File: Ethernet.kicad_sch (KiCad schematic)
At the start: 47 parts, among them J2 RJ45_Hanrun_HR911105A_Horizon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, U2 DP83848C, U3 AMS1117-3.3, Y2 WTL7K85438FO

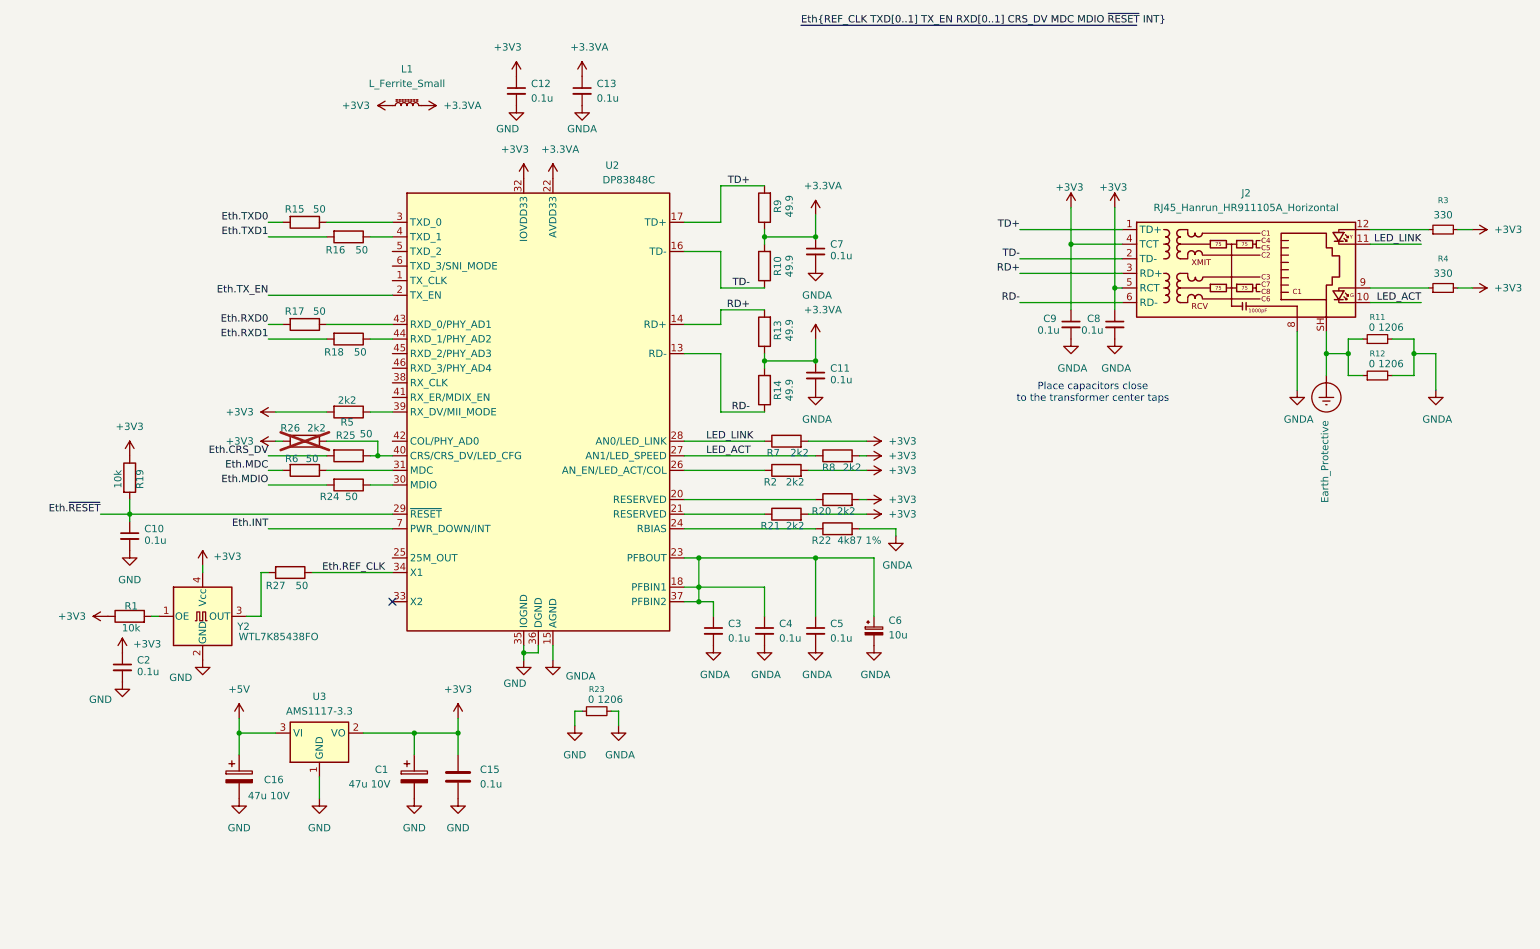
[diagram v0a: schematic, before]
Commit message: Ethernet W55000 controller added
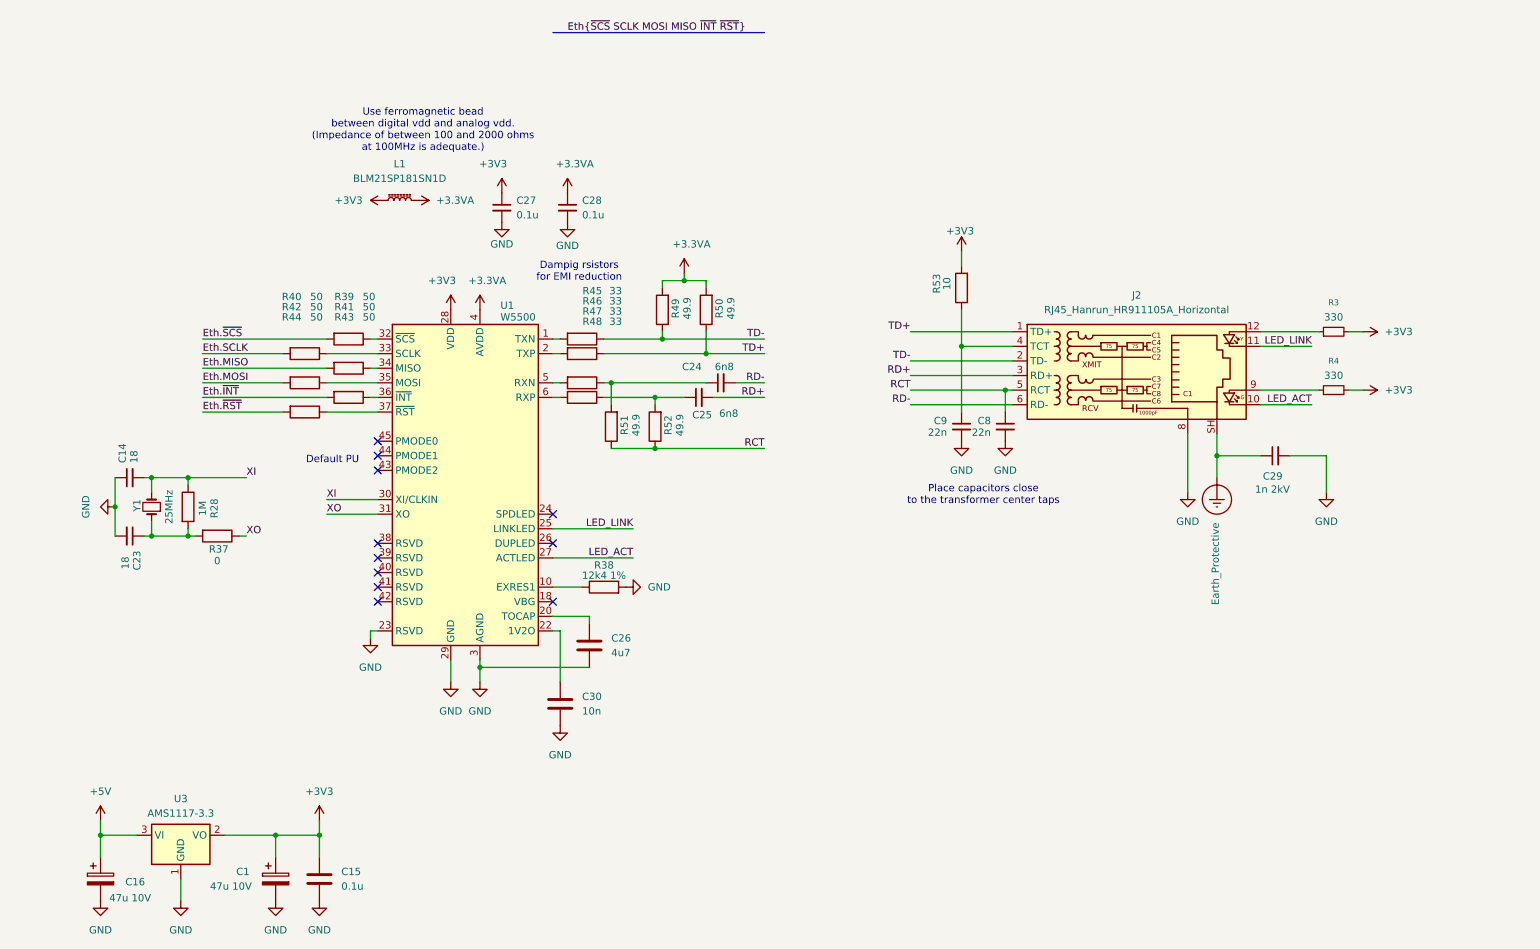
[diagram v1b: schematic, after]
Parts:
- removed C10, C11, C12, C13, C2, C3, C4, C5, C7: 0.1u, symbol Device:C_Small
- removed C6: 10u, symbol Device:C_Polarized_Small
- removed R1, R19: 10k, symbol Device:R
- removed R10, R13, R14, R9: 49.9, symbol Device:R
- removed R11, R12, R23: 0 1206, symbol Device:R_Small
- removed R15, R16, R17, R18, R24, R25, R27, R6: 50, symbol Device:R
- removed R2, R20, R21, R26, R5, R7, R8: 2k2, symbol Device:R
- removed R22: 4k87 1%, symbol Device:R
- removed U2: DP83848C, Package_QFP:LQFP-48_7x7mm_P0.5mm, symbol Interface_Ethernet:DP83848C
- removed Y2: WTL7K85438FO, Oscillator:Oscillator_SMD_SeikoEpson_SG8002CA-4Pin_7.0x5.0mm, symbol Oscillator:SG-7050CCN
- added C14, C23: 18, symbol Device:C_Small
- added C24, C25: 6n8, symbol Device:C_Small
- added C26: 4u7, Capacitor_SMD:C_0805_2012Metric, symbol Device:C
- added C27, C28: 0.1u, symbol Device:C_Small
- added C29: 1n 2kV, Capacitor_THT:C_Disc_D7.5mm_W5.0mm_P7.50mm, symbol Device:C_Small
- added C30: 10n, Capacitor_SMD:C_0805_2012Metric, symbol Device:C
- added R28: 1M, Resistor_SMD:R_0805_2012Metric, symbol Device:R
- added R37: 0, Resistor_SMD:R_0805_2012Metric, symbol Device:R
- added R38: 12k4 1%, Resistor_SMD:R_0805_2012Metric, symbol Device:R
- added R39, R40, R41, R42, R43, R44: 50, Resistor_SMD:R_0805_2012Metric, symbol Device:R
- added R45, R46, R47, R48: 33, Resistor_SMD:R_0805_2012Metric, symbol Device:R
- added R49, R50, R51, R52: 49.9, Resistor_SMD:R_0805_2012Metric, symbol Device:R
- added R53: 10, Resistor_SMD:R_0805_2012Metric, symbol Device:R
- added U1: W5500, Package_QFP:LQFP-48_7x7mm_P0.5mm, symbol Interface_Ethernet:W5500
- added Y1: 25MHz, PCM_SparkFun-Clock:Crystal-SMD-5x3.2mm, symbol PCM_SparkFun-Clock:Crystal
- C8, C9: value 0.1u -> 22n
- L1: value L_Ferrite_Small -> BLM21SP181SN1D; footprint (none) -> Inductor_SMD:L_0805_2012Metric
- R3, R4: footprint (none) -> Resistor_SMD:R_0805_2012Metric
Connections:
- net GNDA is gone; now on net GND: C8.2, C9.2, J2.8
- net +3.3VA: now also C28.1, R49.2, R50.2, U1.11 (AVDD), U1.15 (AVDD), U1.17 (AVDD), U1.21 (AVDD), U1.4 (AVDD), U1.8 (AVDD)
- net +3V3: now also C27.1, R53.2, U1.28 (VDD); no longer C8.1, C9.1, J2.4 (TCT), J2.5 (RCT)
- net Earth_Protective: now also C29.1
- net GND: now also C14.1, C23.2, C26.2, C27.2, C28.2, C29.2, C30.2, R38.2, U1.14 (AGND), U1.16 (AGND), U1.19 (AGND), U1.23 (RSVD), U1.29 (GND), U1.3 (AGND), U1.48 (AGND), U1.9 (AGND)
- net LED_ACT: now also U1.27 (ACTLED)
- net LED_LINK: now also U1.25 (LINKLED)
- net RD+: now also C25.2
- net RD-: now also C24.2
- net TD+: now also R46.1, R50.1
- net TD-: now also R45.1, R49.1
- new net: R39.1, U1.32 (~{SCS})
- new net: C24.1, R47.1, R51.2
- new net: R41.1, U1.34 (MISO)
- new net: C23.1, R28.2, R37.2, Y1.1
- new net: R45.2, U1.1 (TXN)
- new net: C26.1, U1.20 (TOCAP)
- new net: R38.1, U1.10 (EXRES1)
- new net: R46.2, U1.2 (TXP)
- new net: C30.1, U1.22 (1V2O)
- new net: R40.1, U1.33 (SCLK)
- new net: R42.1, U1.35 (MOSI)
- new net: R43.1, U1.36 (~{INT})
- new net: R44.1, U1.37 (~{RST})
- new net: R47.2, U1.5 (RXN)
- new net: R48.2, U1.6 (RXP)
- new net: C25.1, R48.1, R52.2
- new net: C9.1, J2.4 (TCT), R53.1
- new net Eth.MISO: R41.2
- new net Eth.MOSI: R42.2
- new net Eth.SCLK: R40.2
- new net Eth.~{INT}: R43.2
- new net Eth.~{RST}: R44.2
- new net Eth.~{SCS}: R39.2
- new net RCT: C8.1, J2.5 (RCT), R51.1, R52.1
- new net XI: C14.2, R28.1, U1.30 (XI/CLKIN), Y1.2
- new net XO: R37.1, U1.31 (XO)
- no-connect marks 1 -> 11
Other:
- note added: "Dampig rsistors for EMI reduction"
- note added: "Default PU"
- note added: "Use ferromagnetic bead between digital vdd and analog vdd. (Impedance of between 100 and 2000 ohms at 100MHz is adequate.)"
- moved on the sheet: C1, C15, C16, C8, C9, J2, L1, R3, R4, U3
